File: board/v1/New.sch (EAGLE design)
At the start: 28 parts, among them IC2 LTC3525, IC3 MCP1703CB, U3 ATMEGA32U4, X1 USB-MICROB, Y1 16MHz

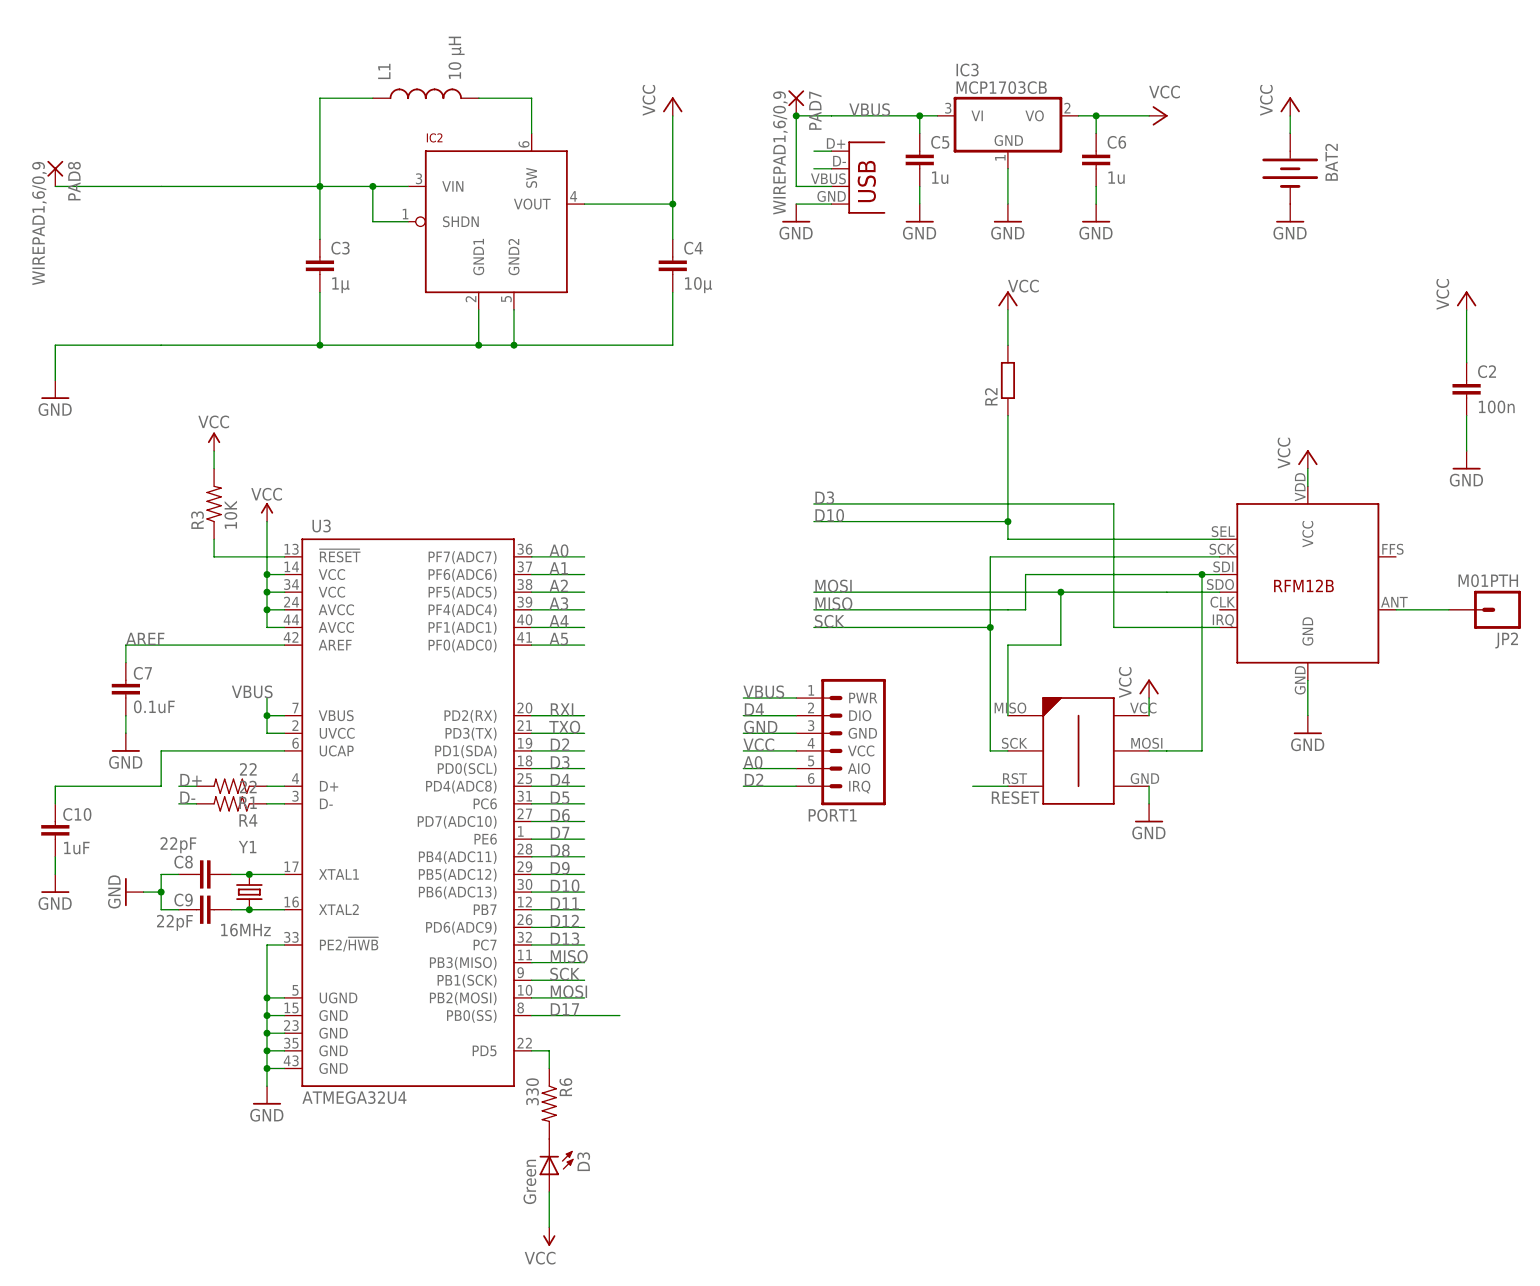
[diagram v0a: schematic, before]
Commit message: PCB revision after the MISO/MOSI pins were messed up
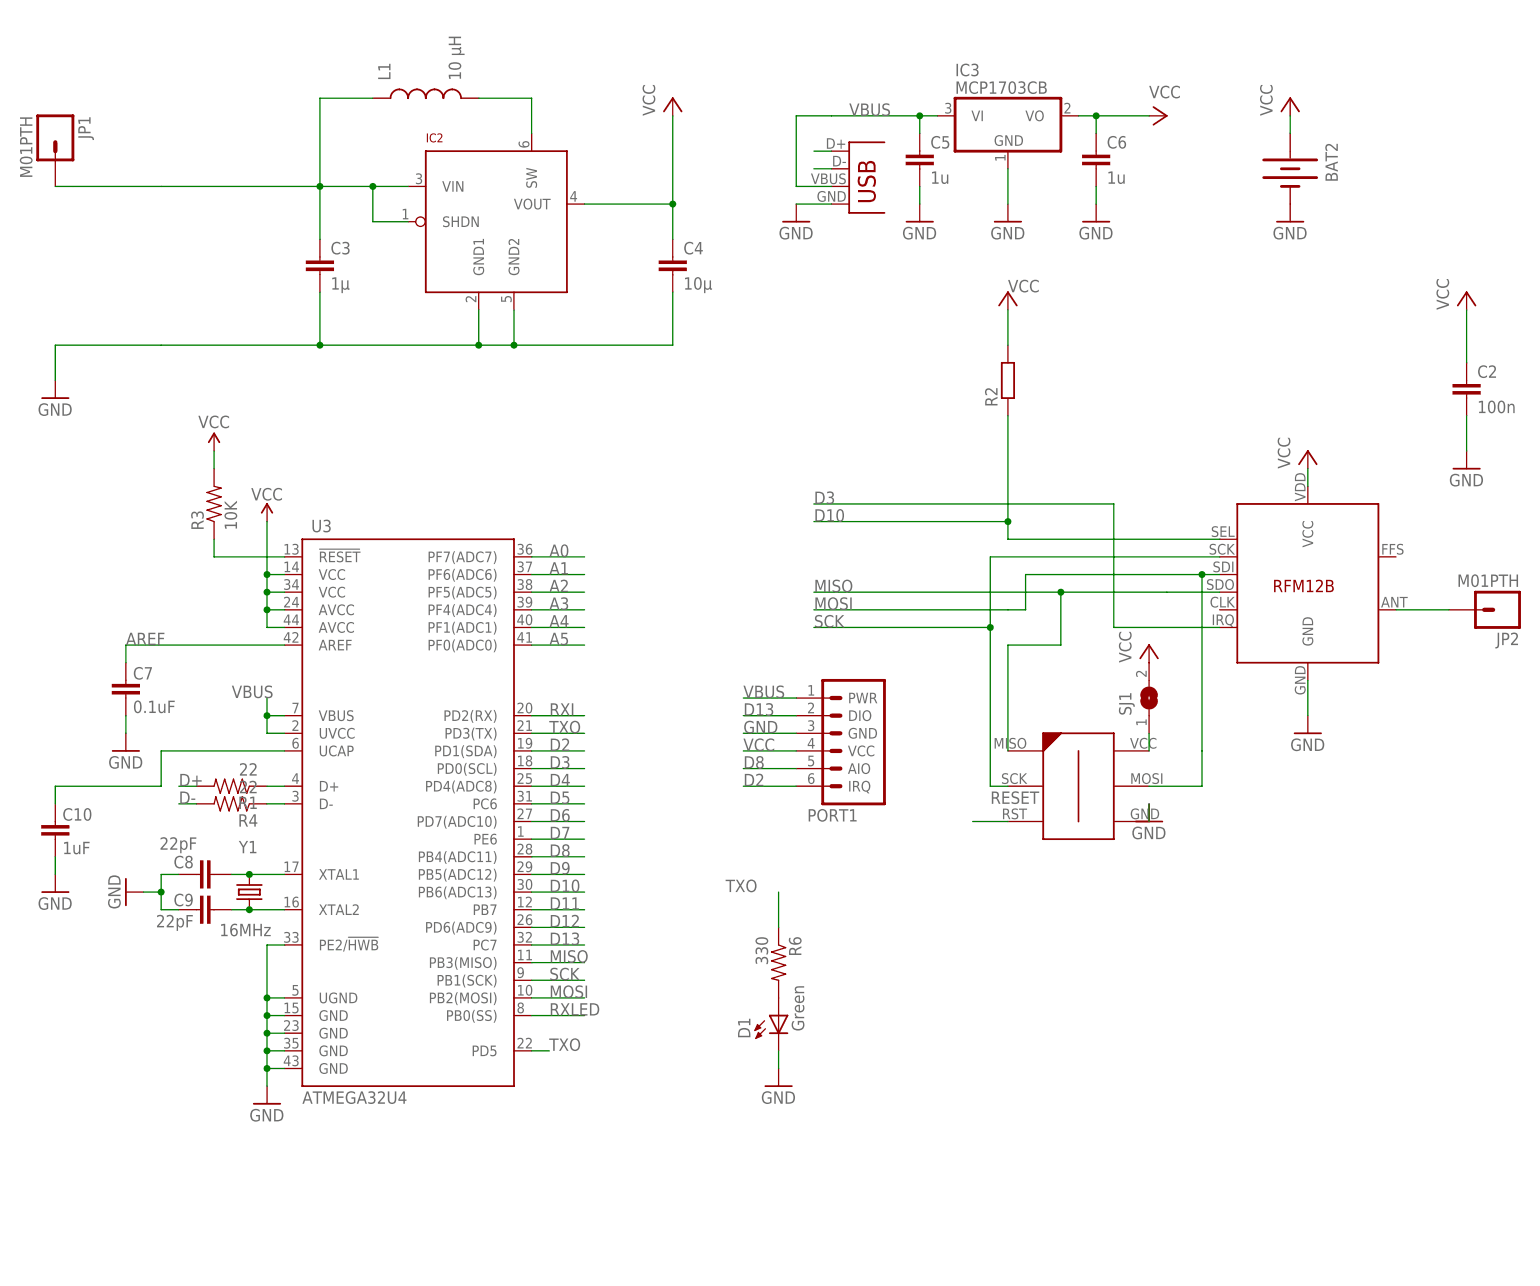
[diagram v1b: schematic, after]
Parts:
- removed D3: Green, SparkFun:LED0603
- removed PAD7, PAD8: WIREPAD1,6/0,9, wirepad:WIREPAD1,6/0,9
- added D1: Green, SparkFun:LED0603
- added JP1: M01PTH, SparkFun:M01PTH
- added SJ1: (no value), jumper:SJ
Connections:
- net D17 renamed RXLED
- removed net TXLED: R6.1, U3.PD5
- new net N$8: U3.PD5
- new net N$9: SJ1.1, U$2.P$6
- net A0: no longer PORT1.AIO
- net D13: now also PORT1.DIO
- net D4: no longer PORT1.DIO
- net D8: now also PORT1.AIO
- net GND: now also D1.C
- net MISO: now also U$1.SDO, U$2.P$1; no longer U$1.SDI, U$2.P$5
- net MOSI: now also U$1.SDI, U$2.P$5; no longer U$1.SDO, U$2.P$1
- net N$6: now also D1.A; no longer D3.C
- net TXO: now also R6.1
- net VBUS: no longer PAD7.P
- net VCC: now also SJ1.2; no longer D3.A, U$2.P$6
- net VIN: now also JP1.1; no longer PAD8.P
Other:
- moved on the sheet: R6
